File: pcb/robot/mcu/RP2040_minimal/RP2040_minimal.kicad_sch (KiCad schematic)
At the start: 42 parts, among them J2 Conn_01x05, Q5 SN74AHC125RGYR, U2 W25Q128JVS, U3 RP2040, Y1 ECS-120-8-36-CKM-TR3

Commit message: Modularized usb-pd board and main board split
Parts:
- renumbered TP18 to TP10, TP18 to TP11, TP18 to TP24, TP18 to TP26, TP18 to TP27, TP18 to TP33

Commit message: Replace SN74AHC125 ADC buffer with passive protection (fixes #14)
The SN74AHC125 is a digital logic buffer, not an analog pass-through
- its push-pull output snaps to a rail based on VIH/VIL threshold
instead of reproducing the sensed voltage, so the ADC0/ADC1 channels
were not measuring anything meaningful through it. Removed Q5
entirely rather than substituting another buffer/analog-switch IC,
since any replacement still needs external current limiting and the
RP2040's own internal clamp diodes already provide that once fault
current is bounded by a high-impedance divider (verified against the
RP2040 datasheet: VPIN abs max = IOVDD+0.5V, 1uA leakage, fault
current ~33uA at 20V via the 510k/100k dividers - negligible).

- Added R9 (510k) / R12 (100k): new divider for VRect (ADC1), which
  previously fed the buffer directly with no scaling/protection at
  all - a separate problem from the buffer itself.
- Kept R16/R17 (USB_V divider) unchanged; explicitly did not apply
  the historical "R17->200k" note, since that would push Vadc to
  5.63V at 20V input, past the RP2040's absolute max pin rating.
- C38/C39: 0.1uF -> 22nF, recalculated for the real ~83.6kOhm
  Thevenin source impedance now driving them directly (no buffer
  isolating it anymore) - targets ~10ms settling per the issue spec.
- R22/R23 and C36/C37 (ADC2/ADC3 front-end, confirmed unused/spare)
  marked DNP - all associated passives per the issue's request.

Net BOM effect: -1 IC, +2 resistors (net cost reduction).
GPIO22 (former shared OE line) is now free - firmware team should be
aware not to enable internal pull-up/down on GPIO26-29, since the
80kOhm-range internal pull is the same order as the divider impedance
and would corrupt the reading.

Verified via ERC/DRC: same 314/7 violation counts as baseline, 0
unconnected items - no regressions, and confirms R9/R12 nets are
actually routed in copper.
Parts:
- removed C35: 0.1uF, robot:C_0402_1005Metric, symbol robot:C
- removed Q5: SN74AHC125RGYR, robot:SN74AHC125RGYR, symbol robot:SN74AHC125RGYR
- added R12: 100k, robot:R_0603_1608Metric, symbol robot:R
- added R9: 510k, robot:R_0603_1608Metric, symbol robot:R
- C36, C37, R22, R23: now not fitted
- C38, C39: value 0.1uF -> 22nF; Manufacturer Samsung -> Murata; Part Number CL05A104KA5NNNC -> GRM155R71H223KA12J; V_Max (none) -> 50V
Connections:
- net ADC0: now also R25.2
- net ADC1: now also R9.1
- net ADC2: now also R23.2
- net ADC3: now also R22.2
- net GND: now also C38.1, C39.1, R12.2; no longer C38.2, C39.2
- net GPIO26_ADC0: now also C39.2; no longer C39.1
- net GPIO27_ADC1: now also C38.2; no longer C38.1
- net at R24.2: now also R12.1, R9.2
- no-connect marks 0 -> 1
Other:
- note added: "SN74AHC125 removed - cannot pass proportional analog voltage (digital logic threshold corrupts the reading). Replaced with passive high-impedance divider + RC filter, relying on RP2040's internal clamp diodes for overvoltage protection (VPIN abs max = IOVDD+0.5V; fault current <40µA via 510k/100k dividers, well under RP2040's clamp current budget). C=22nF sized for ~10ms settling given ~83.6kΩ Th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"
- note removed: "Cap to be as close to pin 14 (VCC) as possible"
- note removed: "This must be held at VIO during startup to prevent floating pins from disrupting startup routine"

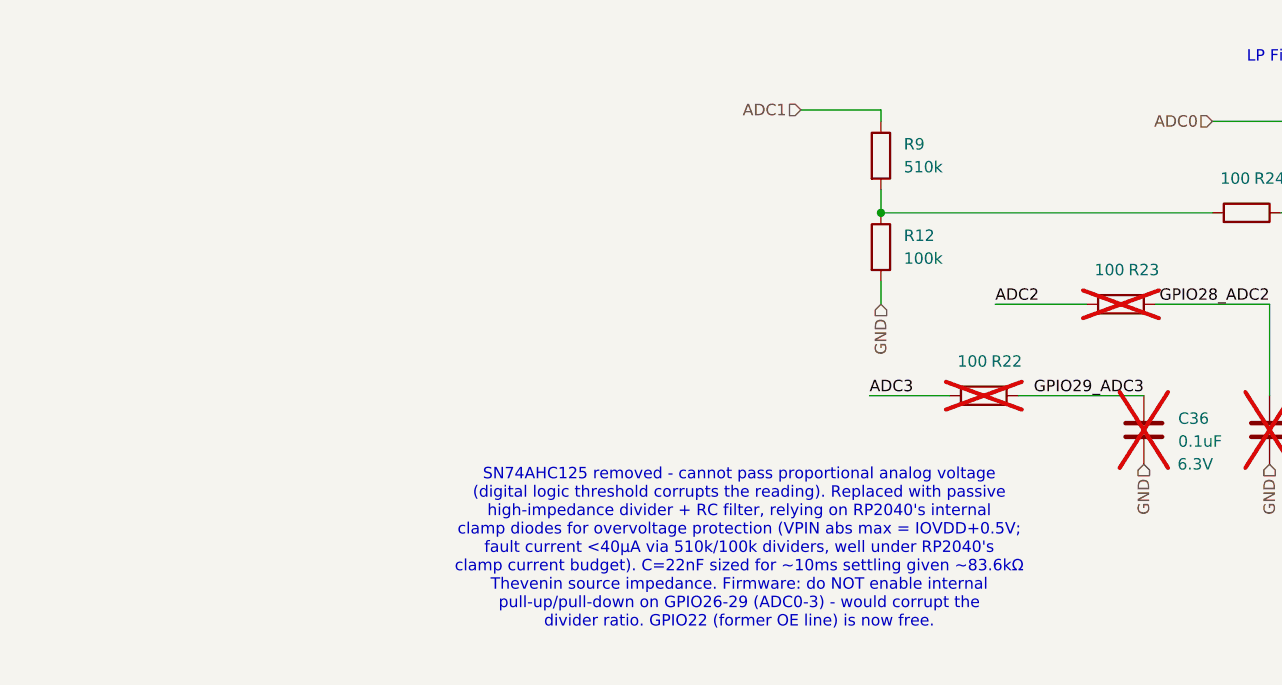
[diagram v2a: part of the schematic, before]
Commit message: Add 470k pull-down on IC1.ON to fix floating pin when off (fixes #6)
Replace DNP C99 (1uF cap) with populated R13 (470kOhm, LCSC C25562) from IC1.ON to GND - was floating when SW1 is open. Sized per TPS22998 worst-case (falling threshold min 0.595V, leakage max 1uA). Verified via ERC/DRC against baseline: no regressions, 0 unconnected items before/after.
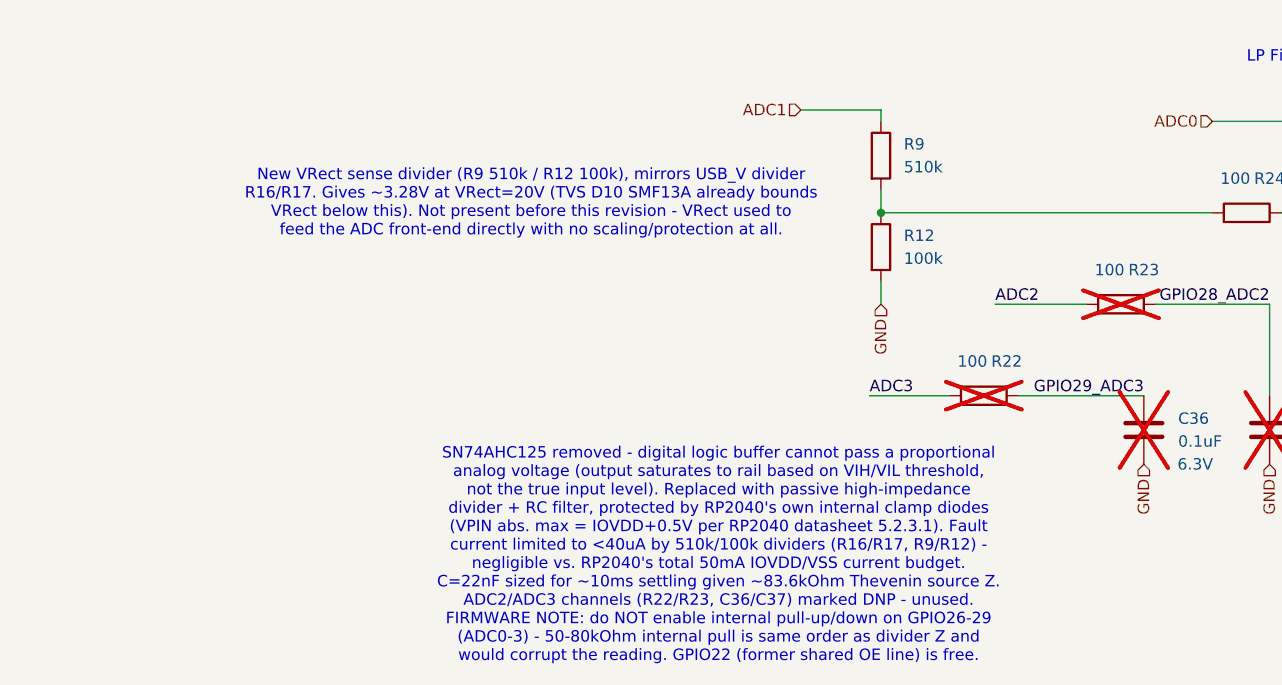
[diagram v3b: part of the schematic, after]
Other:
- note added: "New VRect sense divider (R9 510k / R12 100k), mirrors USB_V divider R16/R17. Gives ~3.28V at VRect=20V (TVS D10 SMF13A already bounds VRect below this). Not present before this revision - VRect used to feed the ADC front-end directly with no scaling/protection at all."
- note added: "SN74AHC125 removed - digital logic buffer cannot pass a proportional analog voltage (output saturates to rail based on VIH/VIL threshold, not the true input level). Replaced with passive high-impedance divider + RC filter, protected by RP2040's own internal clamp diodes (VPIN abs. max = IOVDD+0.5V per RP2040 datasheet 5.2.3.1). Fault current limited to <40uA by 510k/100k dividers (R16/R17, R9/R12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"
- note removed: "SN74AHC125 removed - cannot pass proportional analog voltage (digital logic threshold corrupts the reading). Replaced with passive high-impedance divider + RC filter, relying on RP2040's internal clamp diodes for overvoltage protection (VPIN abs max = IOVDD+0.5V; fault current <40µA via 510k/100k dividers, well under RP2040's clamp current budget). C=22nF sized for ~10ms settling given ~83.6kΩ Th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"
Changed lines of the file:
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@@
 		)
 	)
-	(text "SN74AHC125 removed - cannot pass proportional analog voltage \n(digital logic threshold corrupts the reading). Replaced with passive \nhigh-impedance divider + RC filter, relying on RP2040's internal \nclamp diodes for overvoltage protection (VPIN abs max = IOVDD+0.5V; \nfault current <40µA via 510k/100k dividers, well under RP2040's \nclamp current budget). C=22nF sized for ~10ms settling given ~83.6kΩ \nThevenin source impedance. Firmware: do NOT enable internal \npull-up/pull-down on GPIO26-29 (ADC0-3) - would corrupt the \ndivider ratio. GPIO22 (former OE line) is now free."
+	(text "SN74AHC125 removed - digital logic buffer cannot pass a proportional\nanalog voltage (output saturates to rail based on VIH/VIL threshold,\nnot the true input level). Replaced with passive high-impedance\ndivider + RC filter, protected by RP2040's own internal clamp diodes\n(VPIN abs. max = IOVDD+0.5V per RP2040 datasheet 5.2.3.1). Fault\ncurrent limited to <40uA by 510k/100k dividers (R16/R17, R9/R12) -\nnegligible vs. RP2040's total 50mA IOVDD/VSS current budget.\nC=22nF sized for ~10ms settling given ~83.6kOhm Thevenin source Z.\nADC2/ADC3 channels (R22/R23, C36/C37) marked DNP - unused.\nFIRMWARE NOTE: do NOT enable internal pull-up/down on GPIO26-29\n(ADC0-3) - 50-80kOhm internal pull is same order as divider Z and\nwould corrupt the reading. GPIO22 (former shared OE line) is free."
 		(exclude_from_sim no)
-		(at 277.622 281.178 0)
+		(at 275.336 281.94 0)
 		(effects
 			(font
@@
 		)
 	)
+	(text "New VRect sense divider (R9 510k / R12 100k), mirrors USB_V divider\nR16/R17. Gives ~3.28V at VRect=20V (TVS D10 SMF13A already bounds\nVRect below this). Not present before this revision - VRect used to\nfeed the ADC front-end directly with no scaling/protection at all."
+		(exclude_from_sim no)
+		(at 254.508 242.824 0)
+		(effects
+			(font
+				(size 1.27 1.27)
+			)
+		)
+	)
